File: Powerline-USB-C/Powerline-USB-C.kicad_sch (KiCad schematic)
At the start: 17 parts, among them J1 USB-C 6pin, J2 Eurorack 10pin Power Connector, J3 Eurorack 10pin Power Connector, U1 CH224K, U2 N7812-1C, U3 N7812-1C

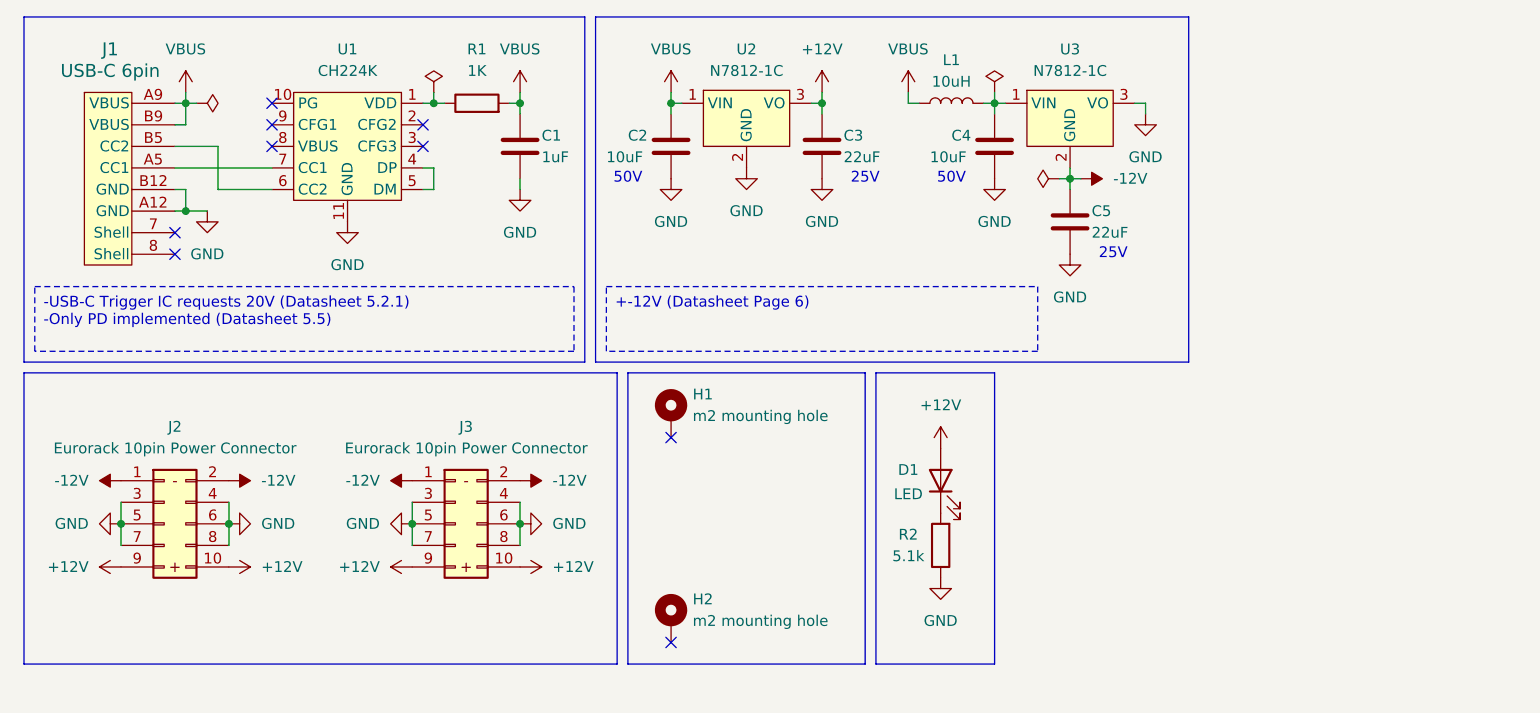
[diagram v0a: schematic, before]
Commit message: minor hardware revision for main PCB
-changed two 10pin headers for singele 16pin header
-added 5V rail
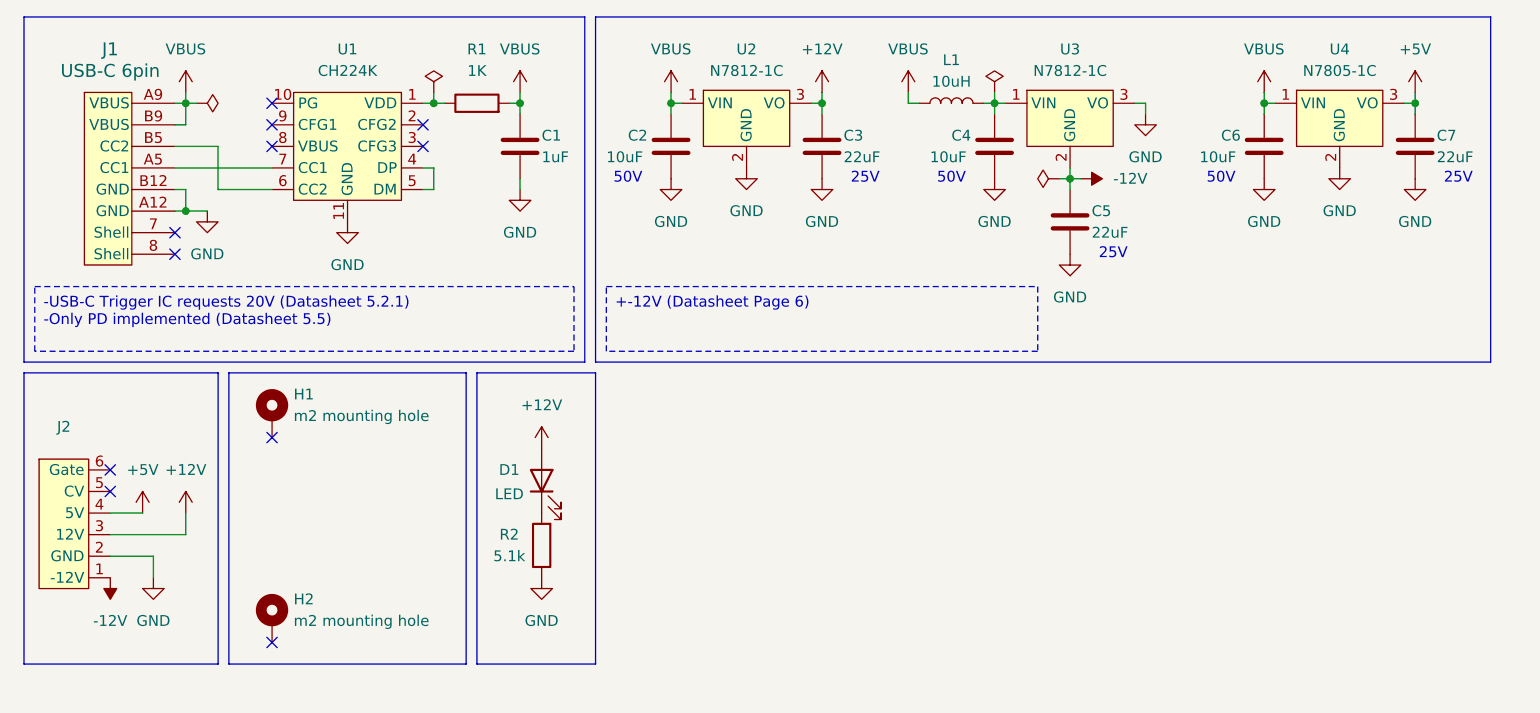
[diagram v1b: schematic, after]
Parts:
- removed J2, J3: Eurorack 10pin Power Connector, Powerline-USB-C:Eurorack shrouded 10 pin SMD header, symbol Powerline-USB-C:Eurorack 10pin Power Connector
- added C6: 10uF, Capacitor_SMD:C_1210_3225Metric, symbol Device:C
- added C7: 22uF, Capacitor_SMD:C_1210_3225Metric, symbol Device:C
- added J2: ~, Powerline-USB-C:Keyed_16pin_Powerheader, symbol Powerline-USB-C:16pin_Power_connector
- added U4: N7805-1C, Powerline-USB-C:N7812-1C, symbol Powerline-USB-C:N7812-1C
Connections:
- net +12V: now also J2.3 (12V)
- net -12V: now also J2.1 (-12V)
- net GND: now also C6.2, C7.2, J2.2 (GND), U4.2 (GND)
- net VBUS: now also C6.1, U4.1 (VIN)
- new net +5V: C7.1, J2.4 (5V), U4.3 (VO)
- no-connect marks 9 -> 11
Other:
- moved on the sheet: D1, H1, H2, R2

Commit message: update to kicad9
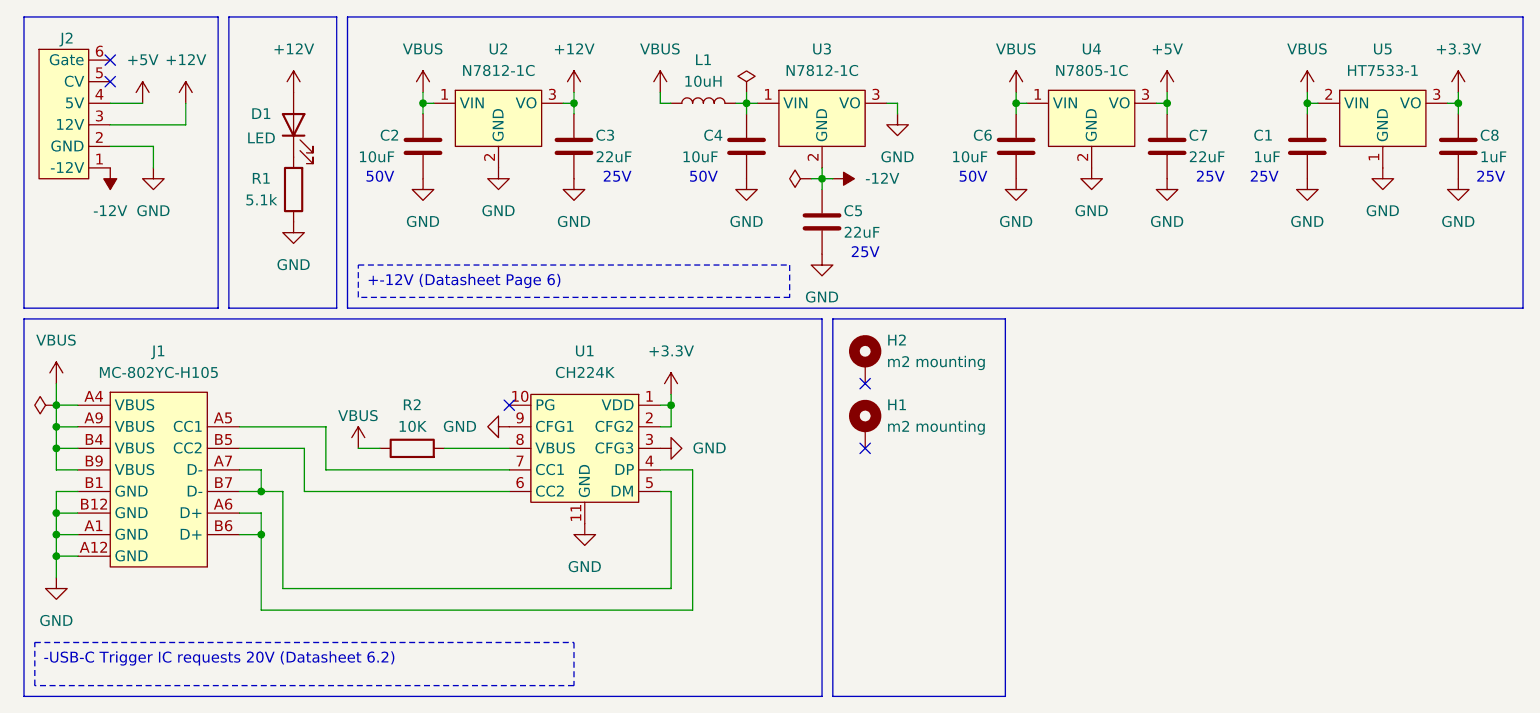
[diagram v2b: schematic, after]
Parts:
- removed J1: USB-C 6pin, Powerline-USB-C:6pin Vertical USB C connector, symbol Powerline-USB-C:Vertical 6pin USB C connector
- removed R1: 1K, Resistor_SMD:R_0603_1608Metric, symbol Device:R
- added C8: 1uF, Capacitor_SMD:C_0805_2012Metric, symbol Device:C
- added J1: MC-802YC-H105, Powerline-USB-C:USB-C, symbol Powerline-USB-C:USB-C
- added R2: 10K, Resistor_SMD:R_0603_1608Metric, symbol Device:R
- added U5: HT7533-1, Powerline-USB-C:HT7533-1, symbol Powerline-USB-C:HT7533-1
- H1, H2: value m2 mounting hole -> m2 mounting
- U1: footprint Package_SO:SSOP-10-1EP_3.9x4.9mm_P1mm_EP2.1x3.3mm_ThermalVias -> Powerline-USB-C:CH224k
- renumbered R2 to R1
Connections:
- net GND: now also U1.3 (CFG3), U1.9 (CFG1), C8.2, J1.A1 (GND), J1.A12 (GND), J1.B1 (GND), J1.B12 (GND), U5.1 (GND)
- net VBUS: now also J1.A4 (VBUS), J1.A9 (VBUS), J1.B4 (VBUS), J1.B9 (VBUS), R2.1, U5.2 (VIN)
- net +3.3V: now reaches U1.1 (VDD)
- net +3.3V: now also U1.2 (CFG2), C8.1, U5.3 (VO)
- net at U1.4 (DP): now also J1.A6 (D+), J1.B6 (D+); no longer U1.5 (DM)
- net at U1.6 (CC2): now also J1.B5 (CC2)
- net at U1.7 (CC1): now also J1.A5 (CC1)
- net at U1.8 (VBUS): now also R2.2
- new net: J1.A7 (D-), J1.B7 (D-), U1.5 (DM)
- no-connect marks 11 -> 5
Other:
- title: Powerlin-USB-C -> Powerline-USB-C
- moved on the sheet: C1, C2, C3, C4, C5, C6, C7, D1, H1, H2, J2, L1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

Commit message: Update to Kicad 9
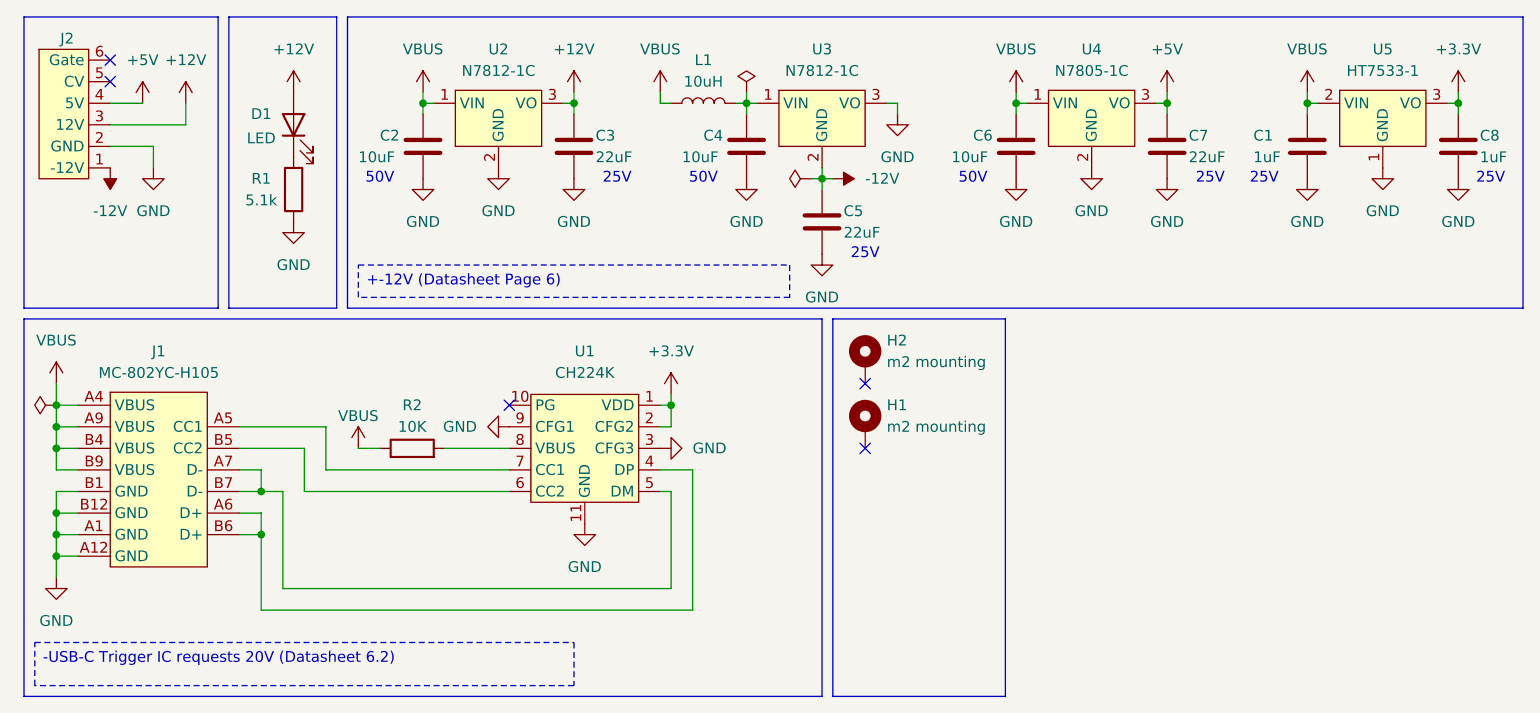
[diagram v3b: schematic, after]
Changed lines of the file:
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@@
 (kicad_sch
-	(version 20231120)
+	(version 20250114)
 	(generator "eeschema")
-	(generator_version "8.0")
+	(generator_version "9.0")
 	(paper "A5")
 	(title_block
@@
 		(rev "0.4")
 	)
+	(rectangle
+		(start 12.7 12.7)
+		(end 35.56 46.99)
+		(stroke
+			(width 0)
+			(type default)
+		)
+		(fill
+			(type none)
+		)
+	)
+	(rectangle
+		(start 50.8 12.7)
+		(end 189.23 46.99)
+		(stroke
+			(width 0)
+			(type default)
+		)
+		(fill
+			(type none)
+		)
+	)
+	(rectangle
+		(start 36.83 12.7)
+		(end 49.53 46.99)
+		(stroke
+			(width 0)
+			(type default)
+		)
+		(fill
+			(type none)
+		)
+	)
+	(rectangle
+		(start 12.7 48.26)
+		(end 106.68 92.71)
+		(stroke
+			(width 0)
+			(type solid)
+		)
+		(fill
+			(type none)
+		)
+	)
+	(rectangle
+		(start 107.95 48.26)
+		(end 128.27 92.71)
+		(stroke
+			(width 0)
+			(type default)
+		)
+		(fill
+			(type none)
+		)
+	)
+	(text "25V"
+		(exclude_from_sim no)
+		(at 152.4 31.75 0)
+		(effects
+			(font
+				(size 1.27 1.27)
+			)
+		)
+	)
+	(text "50V\n"
+		(exclude_from_sim no)
+		(at 92.71 31.75 0)
+		(effects
+			(font
+				(size 1.27 1.27)
+			)
+		)
+	)
+	(text "25V"
+		(exclude_from_sim no)
+		(at 111.76 40.64 0)
+		(effects
+			(font
+				(size 1.27 1.27)
+			)
+		)
+	)
+	(text "25V"
+		(exclude_from_sim no)
+		(at 82.55 31.75 0)
+		(effects
+			(font
+				(size 1.27 1.27)
+			)
+		)
+	)
+	(text "50V\n"
+		(exclude_from_sim no)
+		(at 54.61 31.75 0)
+		(effects
+			(font
+				(size 1.27 1.27)
+			)
+		)
+	)
+	(text "50V\n"
+		(exclude_from_sim no)
+		(at 124.46 31.75 0)
+		(effects
+			(font
+				(size 1.27 1.27)
+			)
+		)
+	)
+	(text "25V"
+		(exclude_from_sim no)
+		(at 185.42 31.75 0)
+		(effects
+			(font
+				(size 1.27 1.27)
+			)
+		)
+	)
+	(text "25V"
+		(exclude_from_sim no)
+		(at 158.75 31.75 0)
+		(effects
+			(font
+				(size 1.27 1.27)
+			)
+		)
+	)
+	(text_box "-USB-C Trigger IC requests 20V (Datasheet 6.2)"
+		(exclude_from_sim no)
+		(at 13.97 86.36 0)
+		(size 63.5 5.08)
+		(margins 0.9525 0.9525 0.9525 0.9525)
+		(stroke
+			(width 0)
+			(type dot)
+		)
+		(fill
+			(type none)
+		)
+		(effects
+			(font
+				(size 1.27 1.27)
+			)
+			(justify left top)
+		)
+	)
+	(text_box "+-12V (Datasheet Page 6)"
+		(exclude_from_sim no)
+		(at 52.07 41.91 0)
+		(size 50.8 3.81)
+		(margins 0.9525 0.9525 0.9525 0.9525)
+		(stroke
+			(width 0)
+			(type dot)
+		)
+		(fill
+			(type none)
+		)
+		(effects
+			(font
+				(size 1.27 1.27)
+			)
+			(justify left top)
+		)
+	)
 	(junction
 		(at 16.51 71.12)
@@
 		)
 	)
-	(rectangle
-		(start 12.7 12.7)
-		(end 35.56 46.99)
-		(stroke
-			(width 0)
-			(type default)
-		)
-		(fill
-			(type none)
-		)
-	)
-	(rectangle
-		(start 50.8 12.7)
-		(end 189.23 46.99)
-		(stroke
-			(width 0)
-			(type default)
-		)
-		(fill
-			(type none)
-		)
-	)
-	(rectangle
-		(start 36.83 12.7)
-		(end 49.53 46.99)
-		(stroke
-			(width 0)
-			(type default)
-		)
-		(fill
-			(type none)
-		)
-	)
-	(rectangle
-		(start 12.7 48.26)
-		(end 106.68 92.71)
-		(stroke
-			(width 0)
-			(type solid)
-		)
-		(fill
-			(type none)
-		)
-	)
-	(rectangle
-		(start 107.95 48.26)
-		(end 128.27 92.71)
-		(stroke
-			(width 0)
-			(type default)
-		)
-		(fill
-			(type none)
-		)
-	)
-	(text_box "-USB-C Trigger IC requests 20V (Datasheet 6.2)"
-		(exclude_from_sim no)
-		(at 13.97 86.36 0)
-		(size 63.5 5.08)
-		(stroke
-			(width 0)
-			(type dot)
-		)
-		(fill
-			(type none)
-		)
-		(effects
-			(font
-				(size 1.27 1.27)
-			)
-			(justify left top)
-		)
-	)
-	(text_box "+-12V (Datasheet Page 6)"
-		(exclude_from_sim no)
-		(at 52.07 41.91 0)
-		(size 50.8 3.81)
-		(stroke
-			(width 0)
-			(type dot)
-		)
-		(fill
-			(type none)
-		)
-		(effects
-			(font
-				(size 1.27 1.27)
-			)
-			(justify left top)
-		)
-	)
-	(text "25V"
-		(exclude_from_sim no)
-		(at 152.4 31.75 0)
-		(effects
-			(font
-				(size 1.27 1.27)
-			)
-		)
-	)
-	(text "50V\n"
-		(exclude_from_sim no)
-		(at 92.71 31.75 0)
-		(effects
-			(font
-				(size 1.27 1.27)
-			)
-		)
-	)
-	(text "25V"
-		(exclude_from_sim no)
-		(at 111.76 40.64 0)
-		(effects
-			(font
-				(size 1.27 1.27)
-			)
-		)
-	)
-	(text "25V"
-		(exclude_from_sim no)
-		(at 82.55 31.75 0)
-		(effects
-			(font
-				(size 1.27 1.27)
-			)
-		)
-	)
-	(text "50V\n"
-		(exclude_from_sim no)
-		(at 54.61 31.75 0)
-		(effects
-			(font
-				(size 1.27 1.27)
-			)
-		)
-	)
-	(text "50V\n"
-		(exclude_from_sim no)
-		(at 124.46 31.75 0)
-		(effects
-			(font
-				(size 1.27 1.27)
-			)
-		)
-	)
-	(text "25V"
-		(exclude_from_sim no)
-		(at 185.42 31.75 0)
-		(effects
-			(font
-				(size 1.27 1.27)
-			)
-		)
-	)
-	(text "25V"
-		(exclude_from_sim no)
-		(at 158.75 31.75 0)
-		(effects
-			(font
-				(size 1.27 1.27)
-			)
-		)
-	)
 	(symbol
 		(lib_id "Device:C")
@@
 		)
 		(property "Value" "m2 mounting"
-			(at 114.3 60.9599 0)
+			(at 114.3 60.96 0)
 			(effects
 				(font
@@
 		)
 		(property "Value" "m2 mounting"
-			(at 114.3 53.3399 0)
+			(at 114.3 53.34 0)
 			(effects
 				(font
@@
 		)
 	)
+	(embedded_fonts no)
 )
